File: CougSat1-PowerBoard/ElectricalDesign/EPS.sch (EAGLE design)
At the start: 426 parts, among them J1 Deployable 0, J10 Battery -, J11 PGND, J12 Battery +, J13 VBatt, J2 PV0, J3 PV1, J4 Umbilical, J5 CougSat Card, J6 SWD, J7 PV2, J8 PV3, J9 Deployable 1, Q1 CSD25402Q3A, Q10 CSD25402Q3A, Q11 DMN53D0LDW, Q12 CSD25402Q3A, Q13 DMN53D0LDW, Q14 CSD25402Q3A, Q15 DMN53D0LDW, Q16 CSD25402Q3A, Q17 CSD25402Q3A, Q18 CSD25402Q3A, Q19 DMN53D0LDW, Q2 DMN2008LFU, Q20 CSD25402Q3A, Q21 CSD25402Q3A, Q22 CSD25402Q3A, Q23 DMN53D0LDW, Q24 CSD25402Q3A, Q25 DMN53D0LDW, Q26 CSD25402Q3A, Q27 DMN53D0LDW, Q28 CSD25402Q3A, Q29 CSD25402Q3A, Q3 DMN2008LFU, Q30 CSD25402Q3A, Q31 DMN53D0LDW, Q32 CSD25402Q3A, Q33 DMN53D0LDW, Q34 CSD25402Q3A, Q35 CSD25402Q3A, Q36 DMN53D0LDW, Q37 CSD25402Q3A, Q38 CSD25402Q3A, Q39 DMN53D0LDW, Q4 CSD25402Q3A, Q40 CSD25402Q3A, Q41 CSD25402Q3A, Q42 DMN53D0LDW, Q43 CSD25402Q3A, Q5 DMN53D0LDW, Q6 DMN53D0LDW, Q7 CSD25402Q3A, Q8 CSD25402Q3A, Q9 CSD25402Q3A, SW1 ESE24MH1, U1 INA199C2, U10 INA199C2, U11 INA199C1, U12 AD7689, U13 INA199C2, U14 INA199C2, U15 TXS0102DQM, U16 TXS0102DQM, U17 AD8515, U18 BQ29700, U19 INA199C2, U2 AD7689, U20 TXS0102DQM, U21 TXS0102DQM, U22 STM32L476RGT, U23 AD7291, U24 INA199C2, U25 INA199C2, U26 BQ29700, U27 INA199C2, U28 INA199C2, U29 INA199C2, U3 AD8515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

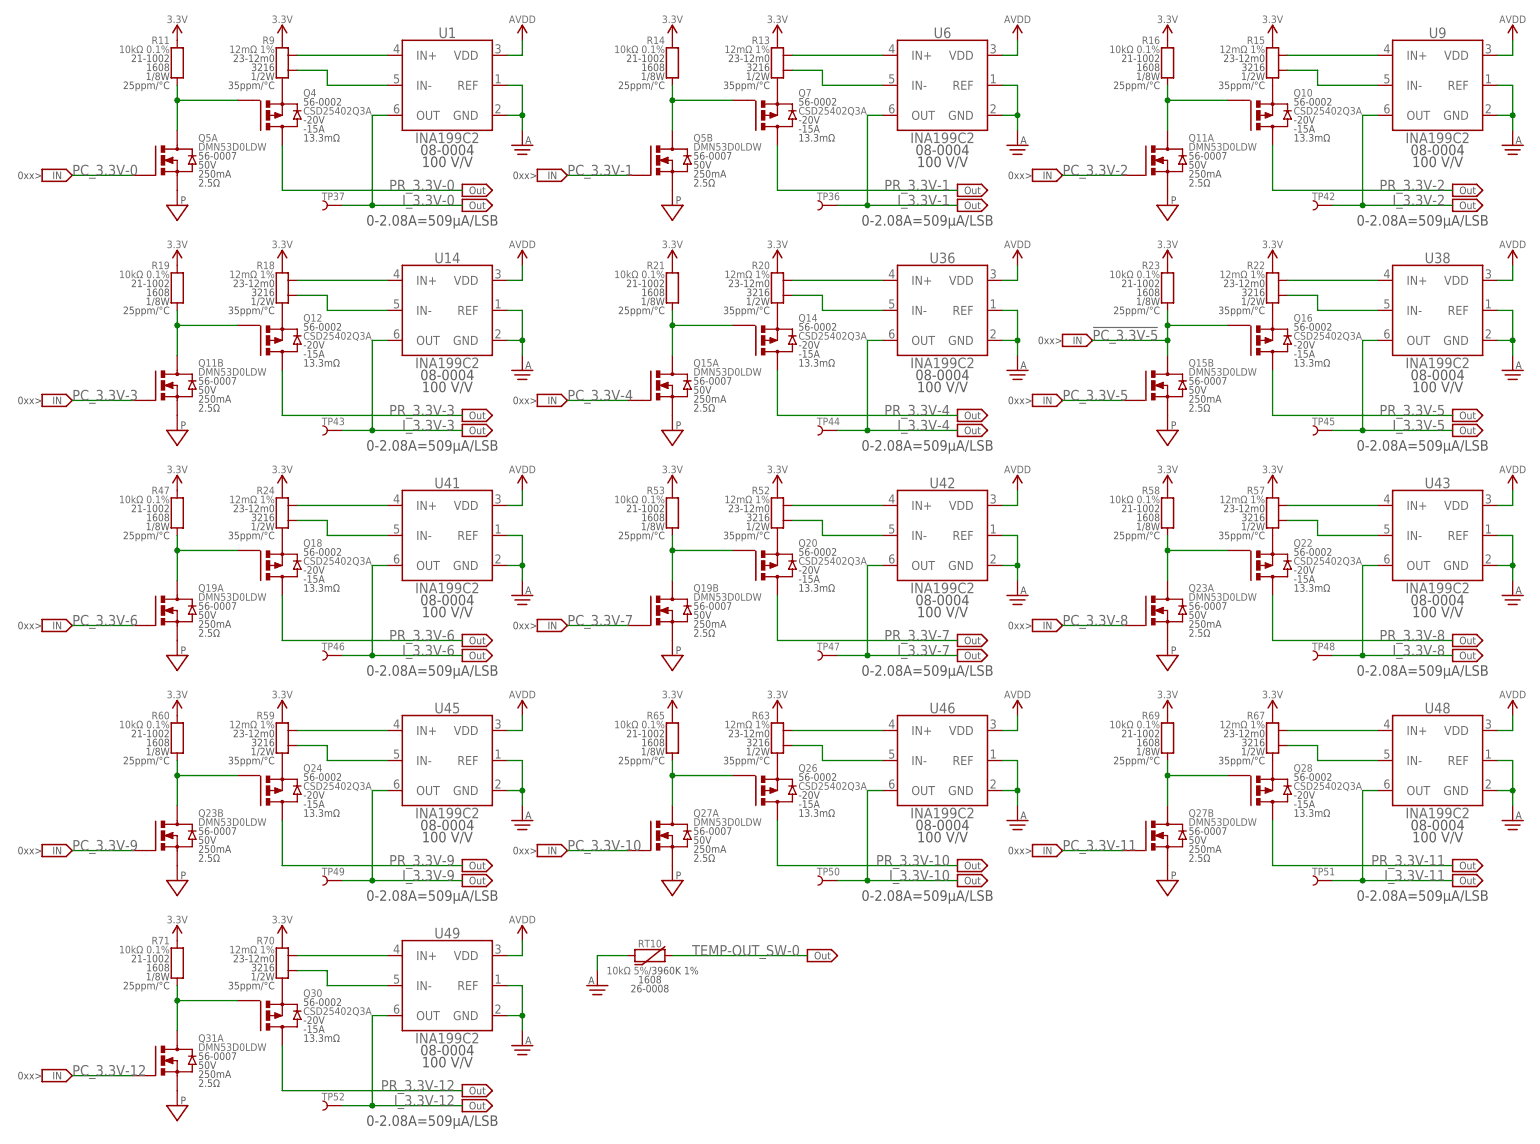
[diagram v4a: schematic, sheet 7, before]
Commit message: Began output current sensing layout
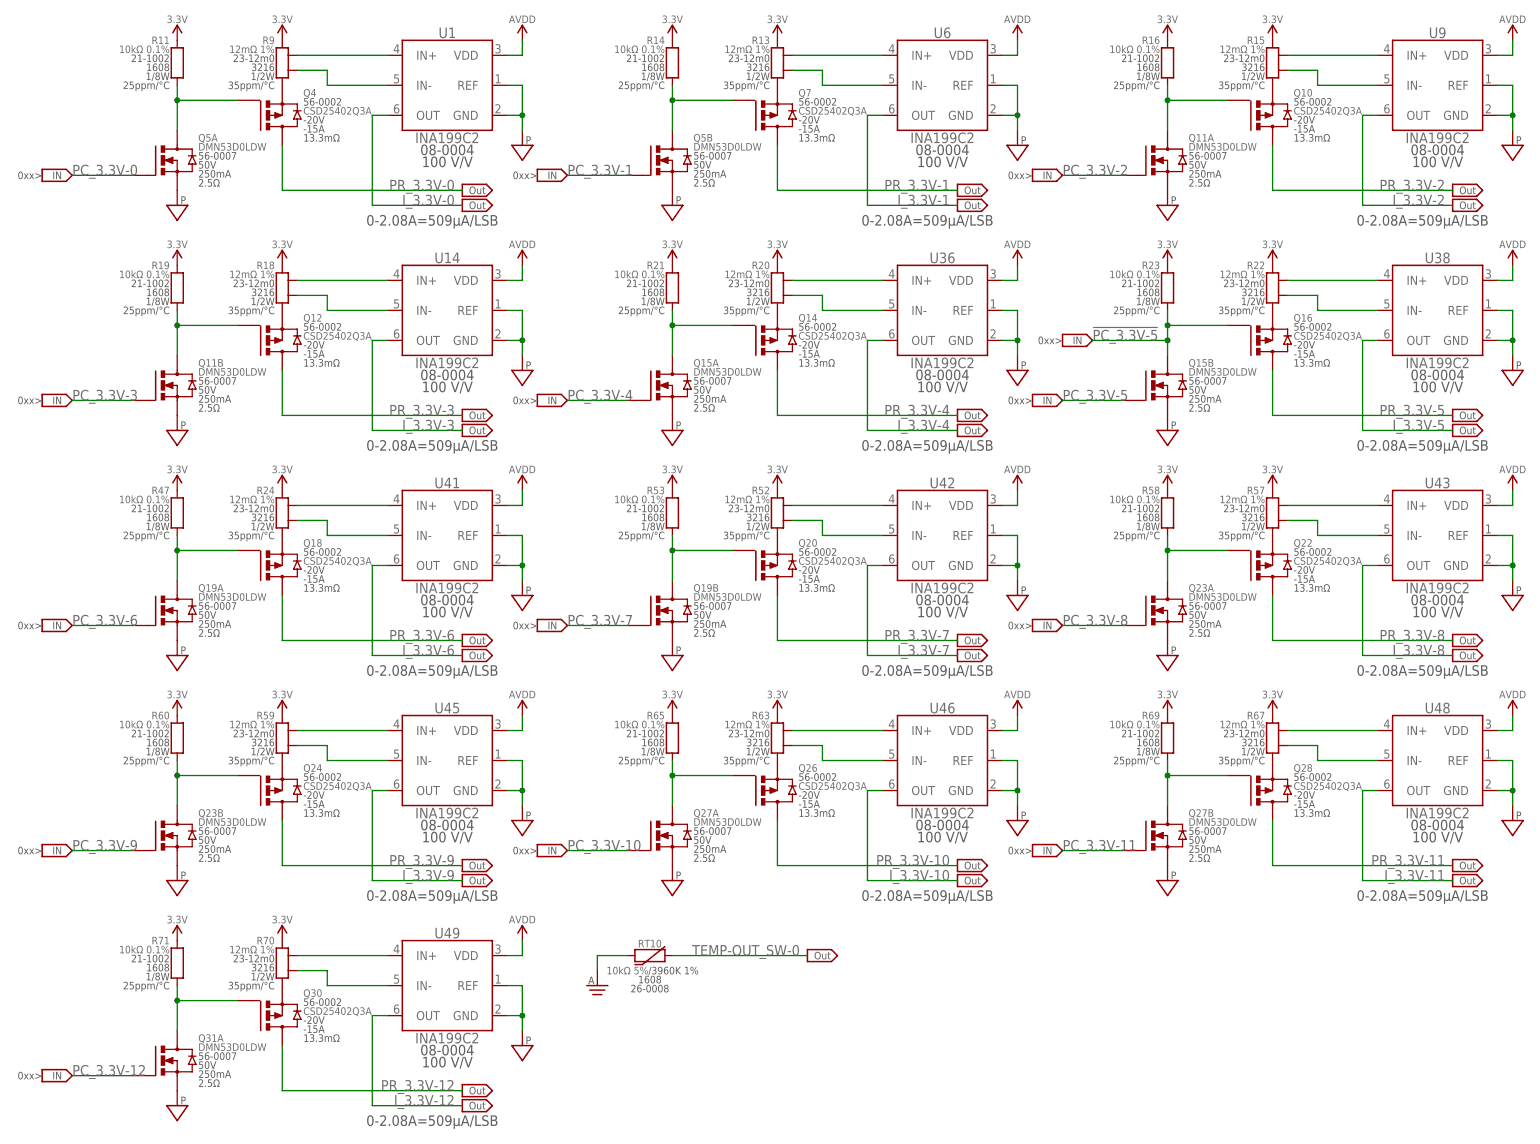
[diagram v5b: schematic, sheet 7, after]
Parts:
- removed TP36, TP37, TP42, TP43, TP44, TP45, TP46, TP47, TP48, TP49, TP50, TP51, TP52, TP53, TP54, TP55, TP56, TP57, TP58, TP59, TP60, TP61, TP62, TP63, TP64: TEST_POINT-SMD-C-1.25, CougsInSpace-Connectors:TEST_POINT-SMD-C-1.25
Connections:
- net BP_VSS-A1 renamed BP_VSS-B
- net AGND: no longer RT10.1, U1.GND, U1.REF, U14.GND, U14.REF, U19.GND, U19.REF, U24.GND, U24.REF, U25.GND, U25.REF, U27.GND, U27.REF, U28.GND, U28.REF, U29.GND, U29.REF, U30.GND, U30.REF, U32.GND, U32.REF, U33.GND, U33.REF, U36.GND, U36.REF, U38.GND, U38.REF, U4.GND, U4.REF, U41.GND, U41.REF, U42.GND, U42.REF, U43.GND, U43.REF, U45.GND, U45.REF, U46.GND, U46.REF, U48.GND, U48.REF, U49.GND, U49.REF, U51.GND, U51.REF, U6.GND, U6.REF, U7.GND, U7.REF, U9.GND, U9.REF
- net I_3.3V-0: no longer TP37.1
- net I_3.3V-1: no longer TP36.1
- net I_3.3V-10: no longer TP50.1
- net I_3.3V-11: no longer TP51.1
- net I_3.3V-12: no longer TP52.1
- net I_3.3V-2: no longer TP42.1
- net I_3.3V-3: no longer TP43.1
- net I_3.3V-4: no longer TP44.1
- net I_3.3V-5: no longer TP45.1
- net I_3.3V-6: no longer TP46.1
- net I_3.3V-7: no longer TP47.1
- net I_3.3V-8: no longer TP48.1
- net I_3.3V-9: no longer TP49.1
- net I_3.3V-PV: no longer TP64.1
- net I_BATT-0: no longer TP53.1
- net I_BATT-1: no longer TP54.1
- net I_BATT-2: no longer TP55.1
- net I_BATT-3: no longer TP56.1
- net I_BATT-4: no longer TP57.1
- net I_BATT-5: no longer TP58.1
- net I_BATT-6: no longer TP59.1
- net I_BH-0: no longer TP60.1
- net I_BH-1: no longer TP61.1
- net I_DP-0: no longer TP62.1
- net I_DP-1: no longer TP63.1
- net PGND: now also RT10.1, U1.GND, U1.REF, U14.GND, U14.REF, U19.GND, U19.REF, U24.GND, U24.REF, U25.GND, U25.REF, U27.GND, U27.REF, U28.GND, U28.REF, U29.GND, U29.REF, U30.GND, U30.REF, U32.GND, U32.REF, U33.GND, U33.REF, U36.GND, U36.REF, U38.GND, U38.REF, U4.GND, U4.REF, U41.GND, U41.REF, U42.GND, U42.REF, U43.GND, U43.REF, U45.GND, U45.REF, U46.GND, U46.REF, U48.GND, U48.REF, U49.GND, U49.REF, U51.GND, U51.REF, U6.GND, U6.REF, U7.GND, U7.REF, U9.GND, U9.REF

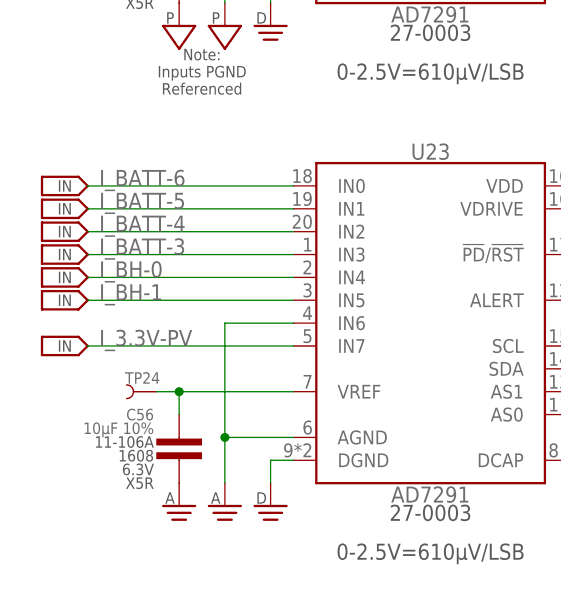
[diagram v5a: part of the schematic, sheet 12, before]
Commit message: Laid out output current sensing
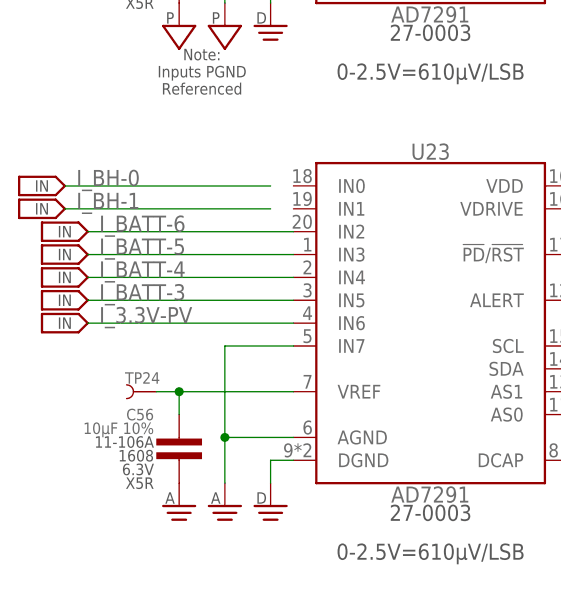
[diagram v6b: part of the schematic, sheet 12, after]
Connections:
- net AGND: now also U23.IN7; no longer U23.IN6
- net I_3.3V-PV: now also U23.IN6; no longer U23.IN7
- net I_BATT-3: now also U23.IN5; no longer U23.IN3
- net I_BATT-4: now also U23.IN4; no longer U23.IN2
- net I_BATT-5: now also U23.IN3; no longer U23.IN1
- net I_BATT-6: now also U23.IN2; no longer U23.IN0
- net I_BH-0: no longer U23.IN4
- net I_BH-1: no longer U23.IN5
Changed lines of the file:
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@@
 <part name="SUPPLY160" library="CougsInSpace-PowerSymbols" deviceset="AGND" device=""/>
 <part name="TP40" library="CougsInSpace-Connectors" deviceset="TEST_POINT" device="-SMD-C-1.25" value="TEST_POINT-SMD-C-1.25"/>
-<part name="OFFSHEET333" library="CougsInSpace-Aesthetics" deviceset="OFF_SHEET-IN" device=""/>
 <part name="SUPPLY278" library="CougsInSpace-PowerSymbols" deviceset="AVREF-1" device=""/>
 <part name="SUPPLY279" library="CougsInSpace-PowerSymbols" deviceset="AVREF-0" device=""/>
@@
 <part name="OFFSHEET242" library="CougsInSpace-Aesthetics" deviceset="OFF_SHEET-OUT" device=""/>
 <part name="OFFSHEET248" library="CougsInSpace-Aesthetics" deviceset="OFF_SHEET-OUT" device=""/>
-<part name="OFFSHEET224" library="CougsInSpace-Aesthetics" deviceset="OFF_SHEET-IN" device=""/>
-<part name="OFFSHEET225" library="CougsInSpace-Aesthetics" deviceset="OFF_SHEET-IN" device=""/>
-<part name="OFFSHEET219" library="CougsInSpace-Aesthetics" deviceset="OFF_SHEET-IN" device=""/>
-<part name="OFFSHEET220" library="CougsInSpace-Aesthetics" deviceset="OFF_SHEET-IN" device=""/>
-<part name="OFFSHEET221" library="CougsInSpace-Aesthetics" deviceset="OFF_SHEET-IN" device=""/>
-<part name="OFFSHEET222" library="CougsInSpace-Aesthetics" deviceset="OFF_SHEET-IN" device=""/>
 <part name="OFFSHEET228" library="CougsInSpace-Aesthetics" deviceset="OFF_SHEET-OUT" device=""/>
 <part name="OFFSHEET155" library="CougsInSpace-Aesthetics" deviceset="OFF_SHEET-OUT" device=""/>
@@
 <part name="SUPPLY288" library="CougsInSpace-PowerSymbols" deviceset="PGND" device=""/>
 <part name="SUPPLY294" library="CougsInSpace-PowerSymbols" deviceset="PGND" device=""/>
+<part name="OFFSHEET224" library="CougsInSpace-Aesthetics" deviceset="OFF_SHEET-IN" device=""/>
+<part name="OFFSHEET225" library="CougsInSpace-Aesthetics" deviceset="OFF_SHEET-IN" device=""/>
+<part name="OFFSHEET219" library="CougsInSpace-Aesthetics" deviceset="OFF_SHEET-IN" device=""/>
+<part name="OFFSHEET220" library="CougsInSpace-Aesthetics" deviceset="OFF_SHEET-IN" device=""/>
+<part name="OFFSHEET221" library="CougsInSpace-Aesthetics" deviceset="OFF_SHEET-IN" device=""/>
+<part name="OFFSHEET222" library="CougsInSpace-Aesthetics" deviceset="OFF_SHEET-IN" device=""/>
+<part name="OFFSHEET333" library="CougsInSpace-Aesthetics" deviceset="OFF_SHEET-IN" device=""/>
 </parts>
 <sheets>
@@
 <instance part="OFFSHEET214" gate="G$1" x="15.24" y="127" smashed="yes"/>
 <instance part="OFFSHEET218" gate="G$1" x="15.24" y="129.54" smashed="yes"/>
-<instance part="OFFSHEET333" gate="G$1" x="15.24" y="58.42" smashed="yes"/>
 <instance part="SUPPLY278" gate="G$1" x="137.16" y="43.18" smashed="yes">
 <attribute name="VALUE" x="137.16" y="46.736" size="1.27" layer="96" align="center"/>
@@
 <attribute name="VALUE" x="137.16" y="110.236" size="1.27" layer="96" align="center"/>
 </instance>
-<instance part="OFFSHEET224" gate="G$1" x="15.24" y="66.04" smashed="yes"/>
-<instance part="OFFSHEET225" gate="G$1" x="15.24" y="63.5" smashed="yes"/>
-<instance part="OFFSHEET219" gate="G$1" x="15.24" y="68.58" smashed="yes"/>
-<instance part="OFFSHEET220" gate="G$1" x="15.24" y="71.12" smashed="yes"/>
-<instance part="OFFSHEET221" gate="G$1" x="15.24" y="73.66" smashed="yes"/>
-<instance part="OFFSHEET222" gate="G$1" x="15.24" y="76.2" smashed="yes"/>
 <instance part="RT5" gate="G$1" x="190.5" y="167.64" smashed="yes" rot="MR0">
 <attribute name="NAME" x="188.722" y="171.958" size="1.27" layer="95" rot="MR0" align="center-left"/>
@@
 </instance>
 <instance part="OFFSHEET165" gate="G$1" x="170.18" y="175.26" smashed="yes"/>
+<instance part="OFFSHEET224" gate="G$1" x="12.7" y="76.2" smashed="yes"/>
+<instance part="OFFSHEET225" gate="G$1" x="12.7" y="73.66" smashed="yes"/>
+<instance part="OFFSHEET219" gate="G$1" x="15.24" y="63.5" smashed="yes"/>
+<instance part="OFFSHEET220" gate="G$1" x="15.24" y="66.04" smashed="yes"/>
+<instance part="OFFSHEET221" gate="G$1" x="15.24" y="68.58" smashed="yes"/>
+<instance part="OFFSHEET222" gate="G$1" x="15.24" y="71.12" smashed="yes"/>
+<instance part="OFFSHEET333" gate="G$1" x="15.24" y="60.96" smashed="yes"/>
 </instances>
 <busses>
@@
 <wire x1="40.64" y1="48.26" x2="33.02" y2="48.26" width="0.1524" layer="91"/>
 <wire x1="33.02" y1="48.26" x2="33.02" y2="43.18" width="0.1524" layer="91"/>
-<pinref part="U23" gate="G$1" pin="IN6"/>
-<wire x1="40.64" y1="60.96" x2="33.02" y2="60.96" width="0.1524" layer="91"/>
-<wire x1="33.02" y1="60.96" x2="33.02" y2="48.26" width="0.1524" layer="91"/>
 <junction x="33.02" y="48.26"/>
+<pinref part="U23" gate="G$1" pin="IN7"/>
+<wire x1="33.02" y1="58.42" x2="33.02" y2="48.26" width="0.1524" layer="91"/>
+<wire x1="40.64" y1="58.42" x2="33.02" y2="58.42" width="0.1524" layer="91"/>
 </segment>
 <segment>
@@
 </segment>
 </net>
-<net name="I_3.3V-PV" class="0">
-<segment>
-<label x="19.05" y="58.42" size="1.778" layer="95"/>
-<wire x1="40.64" y1="58.42" x2="17.78" y2="58.42" width="0.1524" layer="91"/>
-<pinref part="U23" gate="G$1" pin="IN7"/>
-</segment>
-</net>
 <net name="ADC_DCAP-6" class="0">
 <segment>
@@
 <net name="I_BH-0" class="0">
 <segment>
-<wire x1="40.64" y1="66.04" x2="17.78" y2="66.04" width="0.1524" layer="91"/>
-<label x="19.05" y="66.04" size="1.778" layer="95"/>
-<pinref part="U23" gate="G$1" pin="IN4"/>
+<wire x1="38.1" y1="76.2" x2="15.24" y2="76.2" width="0.1524" layer="91"/>
+<label x="16.51" y="76.2" size="1.778" layer="95"/>
 </segment>
 </net>
 <net name="I_BH-1" class="0">
 <segment>
+<wire x1="38.1" y1="73.66" x2="15.24" y2="73.66" width="0.1524" layer="91"/>
+<label x="16.51" y="73.66" size="1.778" layer="95"/>
+</segment>
+</net>
+<net name="I_BATT-3" class="0">
+<segment>
 <wire x1="40.64" y1="63.5" x2="17.78" y2="63.5" width="0.1524" layer="91"/>
 <label x="19.05" y="63.5" size="1.778" layer="95"/>
@@
 </segment>
 </net>
-<net name="I_BATT-3" class="0">
+<net name="I_BATT-4" class="0">
+<segment>
+<wire x1="40.64" y1="66.04" x2="17.78" y2="66.04" width="0.1524" layer="91"/>
+<label x="19.05" y="66.04" size="1.778" layer="95"/>
+<pinref part="U23" gate="G$1" pin="IN4"/>
+</segment>
+</net>
+<net name="I_BATT-5" class="0">
 <segment>
 <wire x1="40.64" y1="68.58" x2="17.78" y2="68.58" width="0.1524" layer="91"/>
@@
 </segment>
 </net>
-<net name="I_BATT-4" class="0">
+<net name="I_BATT-6" class="0">
 <segment>
 <wire x1="40.64" y1="71.12" x2="17.78" y2="71.12" width="0.1524" layer="91"/>
@@
 </segment>
 </net>
-<net name="I_BATT-5" class="0">
-<segment>
-<wire x1="40.64" y1="73.66" x2="17.78" y2="73.66" width="0.1524" layer="91"/>
-<label x="19.05" y="73.66" size="1.778" layer="95"/>
-<pinref part="U23" gate="G$1" pin="IN1"/>
-</segment>
-</net>
-<net name="I_BATT-6" class="0">
+<net name="I_3.3V-PV" class="0">
 <segment>
-<wire x1="40.64" y1="76.2" x2="17.78" y2="76.2" width="0.1524" layer="91"/>
-<label x="19.05" y="76.2" size="1.778" layer="95"/>
-<pinref part="U23" gate="G$1" pin="IN0"/>
+<label x="19.05" y="60.96" size="1.778" layer="95"/>
+<wire x1="40.64" y1="60.96" x2="17.78" y2="60.96" width="0.1524" layer="91"/>
+<pinref part="U23" gate="G$1" pin="IN6"/>
 </segment>
 </net>
